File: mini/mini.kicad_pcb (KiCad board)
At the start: 4 copper layers, 20.1 x 29.4 mm, 19 parts, among them J1 10118194-0001LF, J2 Screw_Terminal_01x03, J3 532610571, U1 ESP32-WROOM-32E, U2 LM3671MF-3.3/NOPB, U3 SN74LVC1T45DBVR

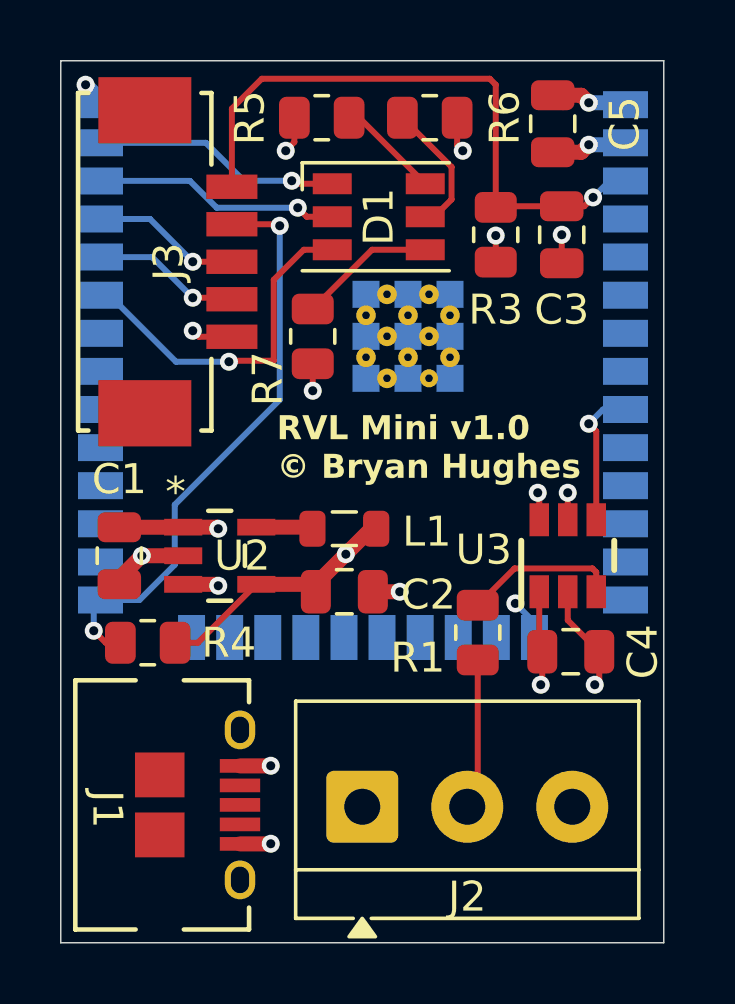
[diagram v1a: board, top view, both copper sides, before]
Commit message: Added missing labels to mini
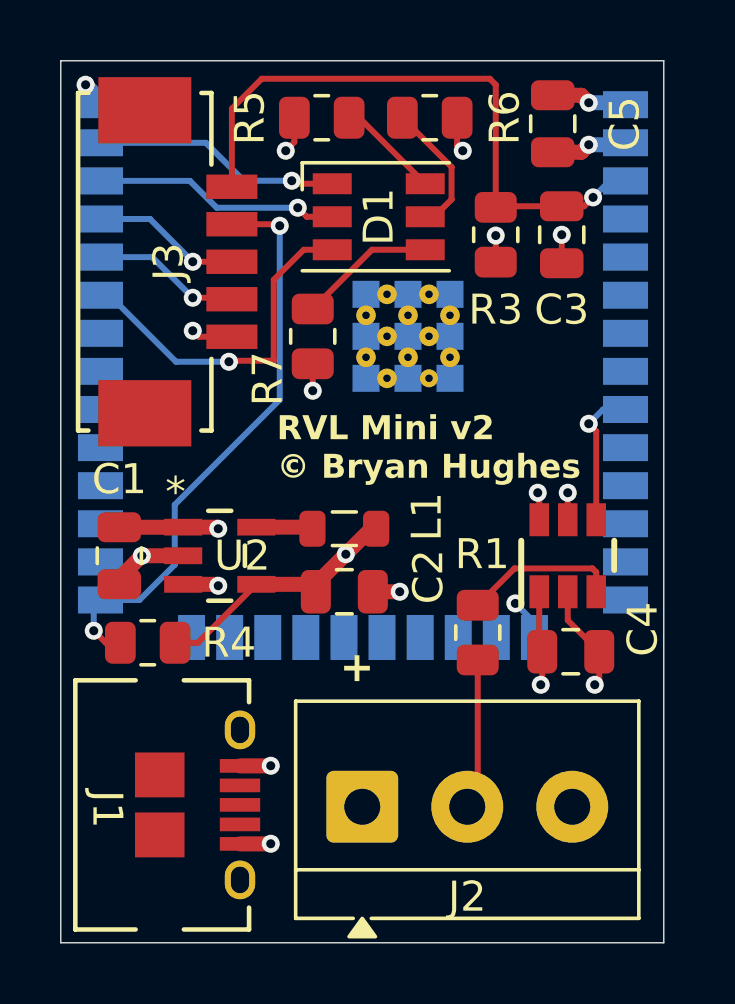
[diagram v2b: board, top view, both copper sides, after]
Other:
- board text added: "+"
- board text added: "5V"
- board text added: "DATA"
- board text added: "GND"
- board text added: "RVL Mini v2 © Bryan Hughes"
- board text removed: "RVL Mini v1.0 © Bryan Hughes"
